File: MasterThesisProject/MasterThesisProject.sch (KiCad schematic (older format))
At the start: 28 parts

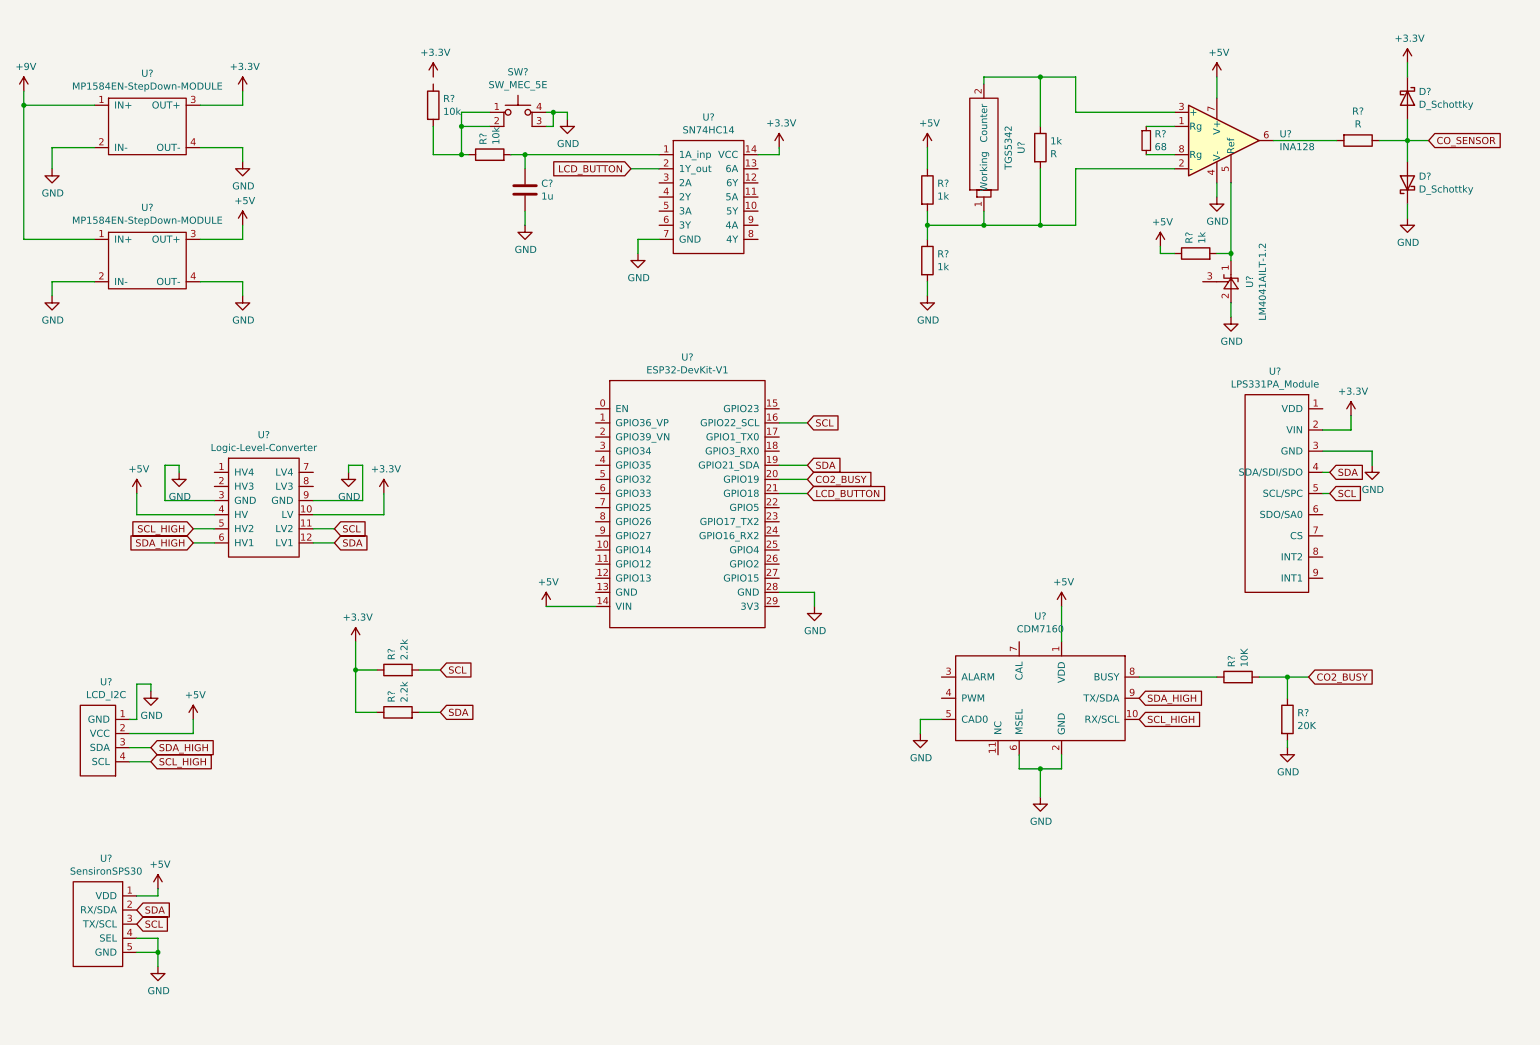
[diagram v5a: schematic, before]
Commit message: Add DHT22 to the schematic
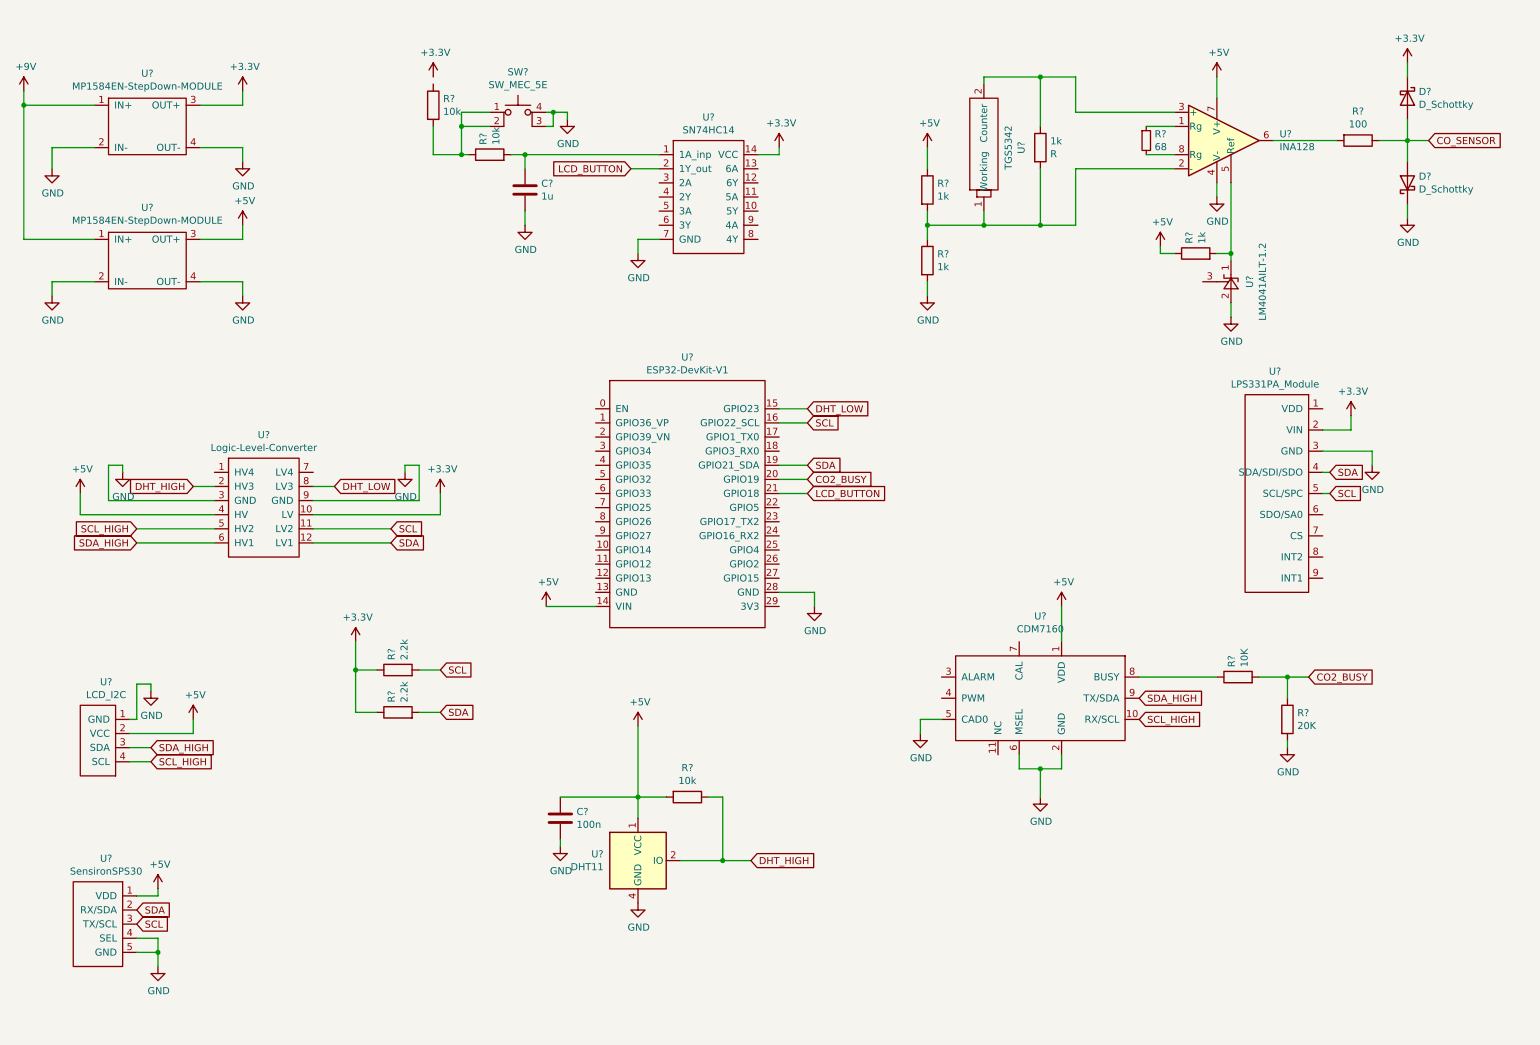
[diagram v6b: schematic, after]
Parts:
- added C?: 100n, symbol Device:C
- added R?: 10k, symbol Device:R
- added U?: DHT11, Sensor:Aosong_DHT11_5.5x12.0_P2.54mm, symbol Sensor:DHT11
- R?: value R -> 100
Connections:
- net +5V: now also C?.1, R?.2, U?.1 (VCC)
- net GND: now also C?.2, U?.4 (GND)
- net DHT_LOW: now reaches U?.15 (GPIO23)
- net DHT_LOW: now also U?.8 (LV3)
- net DHT_HIGH: now reaches U?.2 (HV3)
- net DHT_HIGH: now also R?.1, U?.2 (IO)
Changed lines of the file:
@@
 Wire Wire Line
 	9850 3900 9900 3900
-Wire Wire Line
-	2700 4250 2850 4250
-Wire Wire Line
-	2700 4150 2850 4150
-Text GLabel 2850 4250 2    50   Input ~ 0
+Text GLabel 3250 4250 2    50   Input ~ 0
 SDA
-Text GLabel 2850 4150 2    50   Input ~ 0
+Text GLabel 3250 4150 2    50   Input ~ 0
 SCL
-Wire Wire Line
-	2000 4150 1850 4150
-Wire Wire Line
-	2000 4250 1850 4250
-Text GLabel 1850 4150 0    50   Input ~ 0
+Text GLabel 1450 4150 0    50   Input ~ 0
 SCL_HIGH
-Text GLabel 1850 4250 0    50   Input ~ 0
+Text GLabel 1450 4250 0    50   Input ~ 0
 SDA_HIGH
 $Comp
 L power:+3.3V #PWR?
 U 1 1 60576F46
-P 3200 3900
-F 0 "#PWR?" H 3200 3750 50  0001 C CNN
-F 1 "+3.3V" H 3215 4073 50  0000 C CNN
-F 2 "" H 3200 3900 50  0001 C CNN
-F 3 "" H 3200 3900 50  0001 C CNN
-	1    3200 3900
+P 3600 3900
+F 0 "#PWR?" H 3600 3750 50  0001 C CNN
+F 1 "+3.3V" H 3615 4073 50  0000 C CNN
+F 2 "" H 3600 3900 50  0001 C CNN
+F 3 "" H 3600 3900 50  0001 C CNN
+	1    3600 3900
 	1    0    0    -1
 $EndComp
@@
 L power:+5V #PWR?
 U 1 1 605785E3
-P 1450 3900
-F 0 "#PWR?" H 1450 3750 50  0001 C CNN
-F 1 "+5V" H 1465 4073 50  0000 C CNN
-F 2 "" H 1450 3900 50  0001 C CNN
-F 3 "" H 1450 3900 50  0001 C CNN
-	1    1450 3900
+P 1050 3900
+F 0 "#PWR?" H 1050 3750 50  0001 C CNN
+F 1 "+5V" H 1065 4073 50  0000 C CNN
+F 2 "" H 1050 3900 50  0001 C CNN
+F 3 "" H 1050 3900 50  0001 C CNN
+	1    1050 3900
 	1    0    0    -1
 $EndComp
@@
 L power:GND #PWR?
 U 1 1 6057939A
-P 1750 3750
-F 0 "#PWR?" H 1750 3500 50  0001 C CNN
-F 1 "GND" H 1755 3577 50  0000 C CNN
-F 2 "" H 1750 3750 50  0001 C CNN
-F 3 "" H 1750 3750 50  0001 C CNN
-	1    1750 3750
+P 1350 3750
+F 0 "#PWR?" H 1350 3500 50  0001 C CNN
+F 1 "GND" H 1355 3577 50  0000 C CNN
+F 2 "" H 1350 3750 50  0001 C CNN
+F 3 "" H 1350 3750 50  0001 C CNN
+	1    1350 3750
 	1    0    0    -1
 $EndComp
@@
 L power:GND #PWR?
 U 1 1 6057A370
-P 2950 3750
-F 0 "#PWR?" H 2950 3500 50  0001 C CNN
-F 1 "GND" H 2955 3577 50  0000 C CNN
-F 2 "" H 2950 3750 50  0001 C CNN
-F 3 "" H 2950 3750 50  0001 C CNN
-	1    2950 3750
-	1    0    0    -1
-$EndComp
-Wire Wire Line
-	2000 4050 1450 4050
-Wire Wire Line
-	1450 4050 1450 3900
-Wire Wire Line
-	2700 4050 3200 4050
-Wire Wire Line
-	3200 4050 3200 3900
-Wire Wire Line
-	2950 3750 2950 3700
-Wire Wire Line
-	2950 3700 3050 3700
-Wire Wire Line
-	3050 3700 3050 3950
-Wire Wire Line
-	3050 3950 2700 3950
-Wire Wire Line
-	2000 3950 1650 3950
-Wire Wire Line
-	1650 3950 1650 3700
-Wire Wire Line
-	1650 3700 1750 3700
-Wire Wire Line
-	1750 3700 1750 3750
+P 3350 3750
+F 0 "#PWR?" H 3350 3500 50  0001 C CNN
+F 1 "GND" H 3355 3577 50  0000 C CNN
+F 2 "" H 3350 3750 50  0001 C CNN
+F 3 "" H 3350 3750 50  0001 C CNN
+	1    3350 3750
+	1    0    0    -1
+$EndComp
+Wire Wire Line
+	1050 4050 1050 3900
+Wire Wire Line
+	3600 4050 3600 3900
+Wire Wire Line
+	3350 3750 3350 3700
+Wire Wire Line
+	3350 3700 3450 3700
+Wire Wire Line
+	3450 3700 3450 3950
+Wire Wire Line
+	1250 3950 1250 3700
+Wire Wire Line
+	1250 3700 1350 3700
+Wire Wire Line
+	1350 3700 1350 3750
 $Comp
 L power:GND #PWR?
@@
 P 10100 1400
 F 0 "R?" V 9893 1400 50  0000 C CNN
-F 1 "R" V 9984 1400 50  0000 C CNN
+F 1 "100" V 9984 1400 50  0000 C CNN
 F 2 "" V 10030 1400 50  0001 C CNN
 F 3 "~" H 10100 1400 50  0001 C CNN
@@
 Wire Wire Line
 	10450 1950 10450 1850
+$Comp
+L Sensor:DHT11 U?
+U 1 1 6056B0FC
+P 5000 6500
+F 0 "U?" H 4756 6546 50  0000 R CNN
+F 1 "DHT11" H 4756 6455 50  0000 R CNN
+F 2 "Sensor:Aosong_DHT11_5.5x12.0_P2.54mm" H 5000 6100 50  0001 C CNN
+F 3 "http://akizukidenshi.com/download/ds/aosong/DHT11.pdf" H 5150 6750 50  0001 C CNN
+	1    5000 6500
+	1    0    0    -1
+$EndComp
+$Comp
+L Device:C C?
+U 1 1 60576B16
+P 4450 6200
+F 0 "C?" H 4565 6246 50  0000 L CNN
+F 1 "100n" H 4565 6155 50  0000 L CNN
+F 2 "" H 4488 6050 50  0001 C CNN
+F 3 "~" H 4450 6200 50  0001 C CNN
+	1    4450 6200
+	1    0    0    -1
+$EndComp
+Wire Wire Line
+	5000 5550 5000 6050
+Wire Wire Line
+	5000 6050 4450 6050
+Connection ~ 5000 6050
+Wire Wire Line
+	5000 6050 5000 6200
+Wire Wire Line
+	4450 6350 4450 6400
+$Comp
+L power:GND #PWR?
+U 1 1 60586DF0
+P 4450 6400
+F 0 "#PWR?" H 4450 6150 50  0001 C CNN
+F 1 "GND" H 4455 6227 50  0000 C CNN
+F 2 "" H 4450 6400 50  0001 C CNN
+F 3 "" H 4450 6400 50  0001 C CNN
+	1    4450 6400
+	1    0    0    -1
+$EndComp
+$Comp
+L power:GND #PWR?
+U 1 1 60587CC8
+P 5000 6800
+F 0 "#PWR?" H 5000 6550 50  0001 C CNN
+F 1 "GND" H 5005 6627 50  0000 C CNN
+F 2 "" H 5000 6800 50  0001 C CNN
+F 3 "" H 5000 6800 50  0001 C CNN
+	1    5000 6800
+	1    0    0    -1
+$EndComp
+$Comp
+L Device:R R?
+U 1 1 60588B2C
+P 5350 6050
+F 0 "R?" V 5143 6050 50  0000 C CNN
+F 1 "10k" V 5234 6050 50  0000 C CNN
+F 2 "" V 5280 6050 50  0001 C CNN
+F 3 "~" H 5350 6050 50  0001 C CNN
+	1    5350 6050
+	0    1    1    0
+$EndComp
+$Comp
+L power:+5V #PWR?
+U 1 1 605981E2
+P 5000 5550
+F 0 "#PWR?" H 5000 5400 50  0001 C CNN
+F 1 "+5V" H 5015 5723 50  0000 C CNN
+F 2 "" H 5000 5550 50  0001 C CNN
+F 3 "" H 5000 5550 50  0001 C CNN
+	1    5000 5550
+	1    0    0    -1
+$EndComp
+Wire Wire Line
+	5000 6050 5200 6050
+Wire Wire Line
+	5500 6050 5600 6050
+Wire Wire Line
+	5600 6050 5600 6500
+Wire Wire Line
+	5600 6500 5300 6500
+Wire Wire Line
+	5600 6500 5800 6500
+Connection ~ 5600 6500
+Text GLabel 5800 6500 2    50   Input ~ 0
+DHT_HIGH
+Wire Wire Line
+	1250 3950 2000 3950
+Wire Wire Line
+	1050 4050 2000 4050
+Wire Wire Line
+	1450 4150 2000 4150
+Wire Wire Line
+	1450 4250 2000 4250
+Wire Wire Line
+	2700 3950 3450 3950
+Wire Wire Line
+	2700 4050 3600 4050
+Wire Wire Line
+	2700 4150 3250 4150
+Wire Wire Line
+	2700 4250 3250 4250
+Wire Wire Line
+	2000 3850 1850 3850
+Wire Wire Line
+	2700 3850 2850 3850
+Text GLabel 1850 3850 0    50   Input ~ 0
+DHT_HIGH
+Text GLabel 2850 3850 2    50   Input ~ 0
+DHT_LOW
+Wire Wire Line
+	6200 3300 6000 3300
+Text GLabel 6200 3300 2    50   Input ~ 0
+DHT_LOW
 $EndSCHEMATC

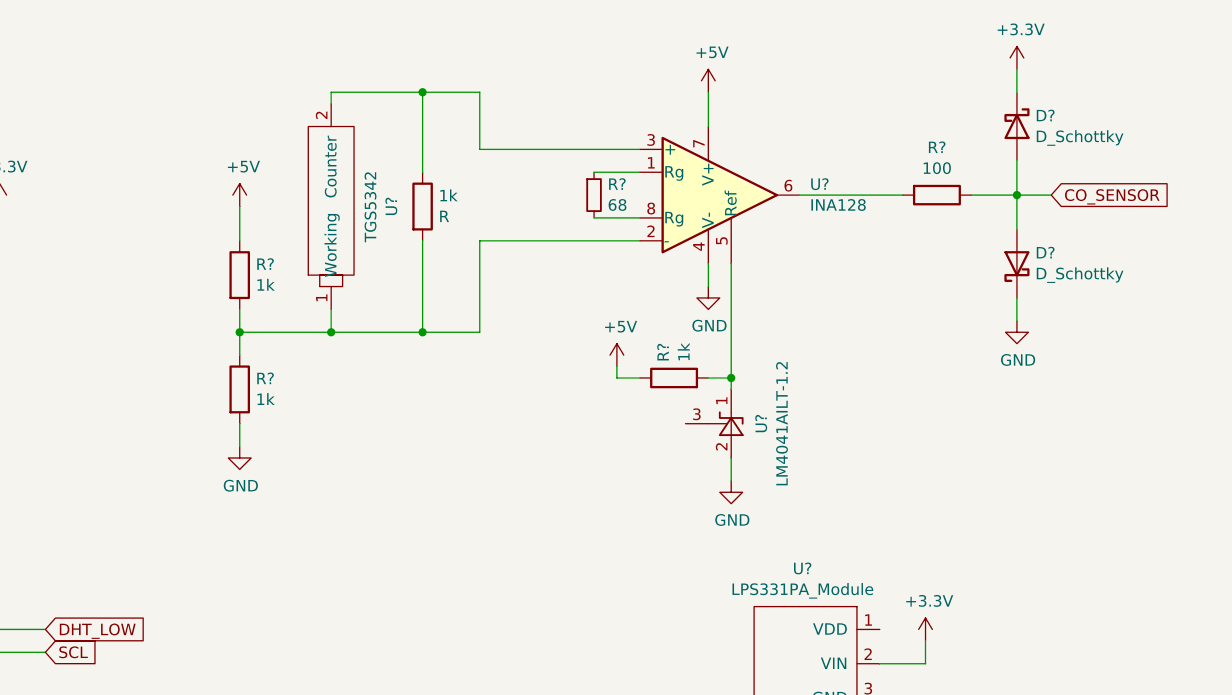
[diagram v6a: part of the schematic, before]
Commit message: Update CO resistor value
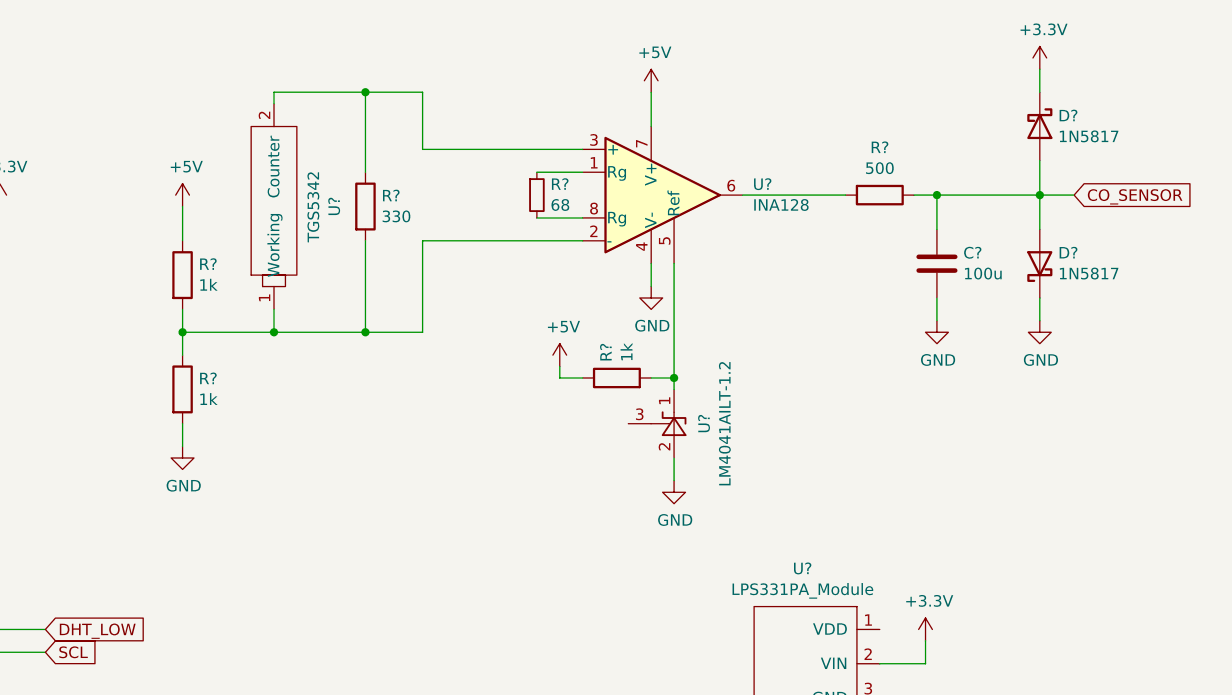
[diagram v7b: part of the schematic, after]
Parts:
- removed D? (x2): D_Schottky, symbol Device:D_Schottky
- added C?: 100u, symbol Device:C
- added D? (x2): 1N5817, Diode_THT:D_DO-41_SOD81_P10.16mm_Horizontal, symbol Diode:1N5817
- R?: renamed from 1k; value R -> 330
- R?: value 100 -> 500
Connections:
- net +3V3: now also D?.1 (K)
- net CO_SENSOR: now also C?.1, D?.2 (A), D?.2 (A)
- net GND: now also C?.2, D?.1 (K)
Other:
- moved on the sheet: R?, U?

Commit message: Add 3.0V source, update CO diodes
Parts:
- removed D? (x2): 1N5817, Diode_THT:D_DO-41_SOD81_P10.16mm_Horizontal, symbol Diode:1N5817
- added C?: 10u, symbol Device:C
- added C?: 0.1u, symbol Device:C
- added C?: 1u, symbol Device:C
- added D? (x2): BAT54J, Diode_SMD:D_SOT-23_ANK, symbol Diode:BAT54J
- added D? (x2): 1N4001, Diode_THT:D_DO-41_SOD81_P10.16mm_Horizontal, symbol Diode:1N4001
- added R?: 3.3k, symbol Device:R
- added R?: 47k, symbol Device:R
- added R?: 4.7k, symbol Device:R
- added R?: 470, symbol Device:R
- added U?: LM317_TO-220, Package_TO_SOT_THT:TO-220-3_Vertical, symbol Regulator_Linear:LM317_TO-220
- R?: value 500 -> 470
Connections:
- net +9V: now also C?.1, D?.1 (K), U?.3 (VI)
- net CO_SENSOR: now also D?.1 (K), D?.2 (A)
- net GND: now also C?.2, C?.2, C?.2, D?.2 (A), R?.2, R?.2, R?.2
- new net: C?.1, D?.2 (A), R?.1, R?.1, R?.2, U?.1 (ADJ)
- new net +3V0: C?.1, D?.1 (K), D?.1 (K), D?.2 (A), R?.1, R?.1, U?.2 (VO)
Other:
- moved on the sheet: R?, U?
